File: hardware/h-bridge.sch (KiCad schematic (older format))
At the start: 78 parts, among them M1 MOUNTING_HOLE, M2 MOUNTING_HOLE, M3 MOUNTING_HOLE, M4 MOUNTING_HOLE, M5 MOUNTING_HOLE, M6 MOUNTING_HOLE, P10 CONN_01_BRK, P11 CONN_01_M+, P12 CONN_01_M-, P8 CONN_01_V+, P9 CONN_01_V-, Q10 PSMN021-100, Q3 IRFP4468, Q4 PSMN021-100, Q5 IRFP4468, Q6 IRFP4468, Q7 IRFP4468, Q8 IRFP4468, Q9 IRFP4468, U16 Si8045AA, U17 MIC4127, U18 MIC4127, U19 LM5102, U20 Si8045AA, U21 LM5102

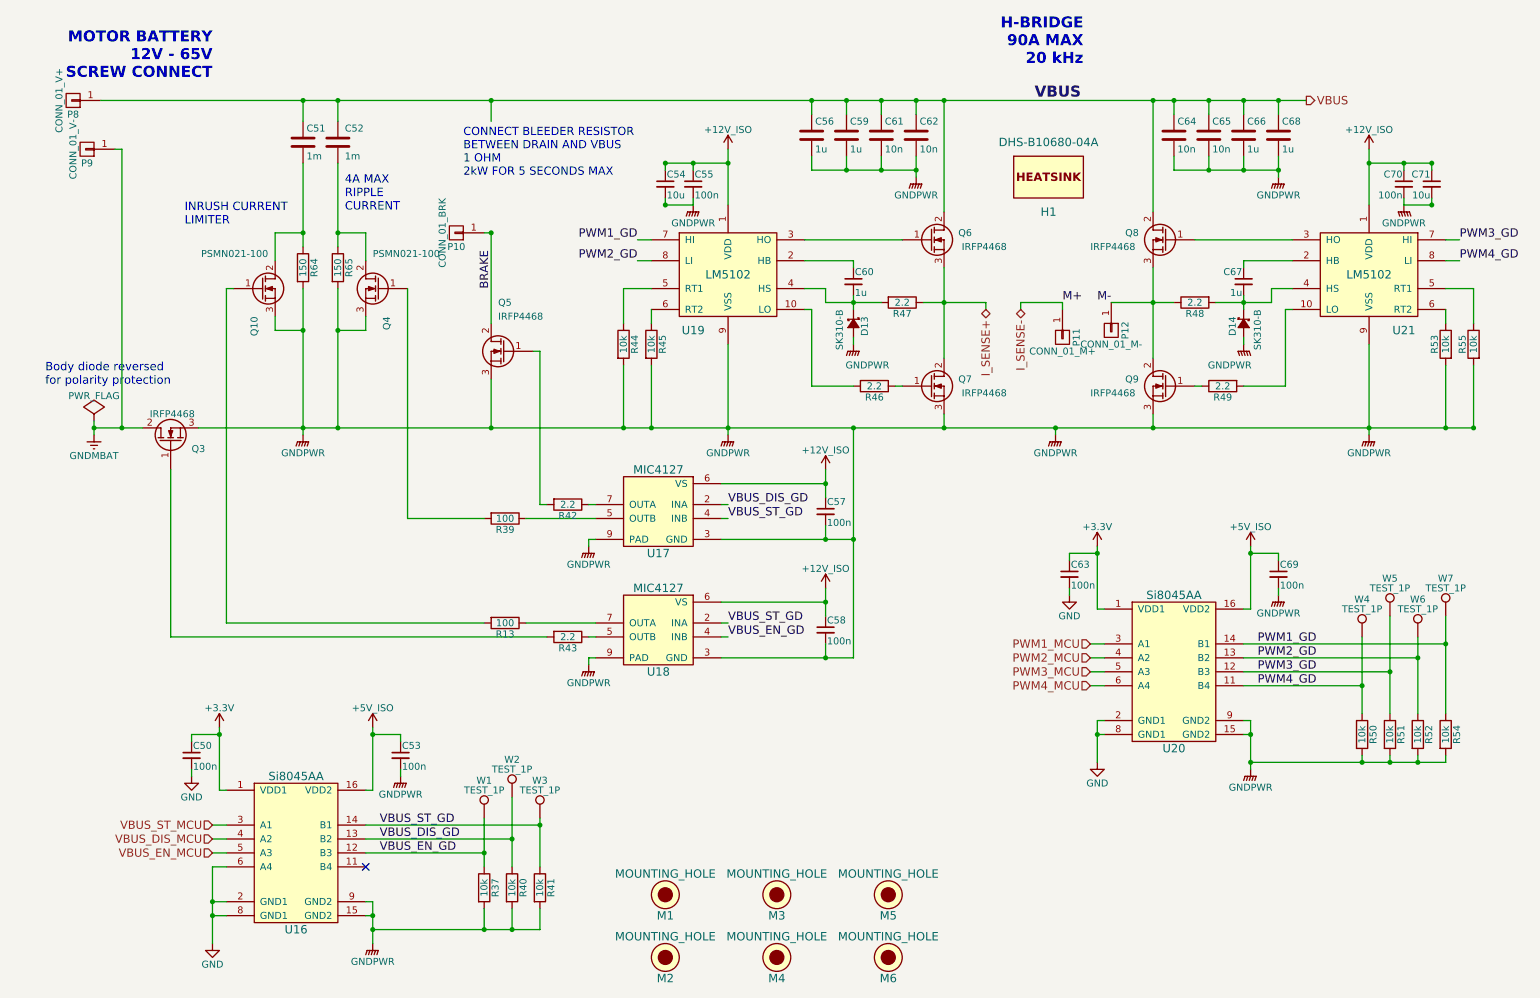
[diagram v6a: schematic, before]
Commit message: Gate driver layout mostly complete
- Gate driver layout
- Switch LM5102 for UCC27211 (higher current, more robust)
- Tweak gate drive circuit passives
- No soldermask on high-current traces
- Fix error in orientation of LAH-100P footprint
- Improved draft layout of control section
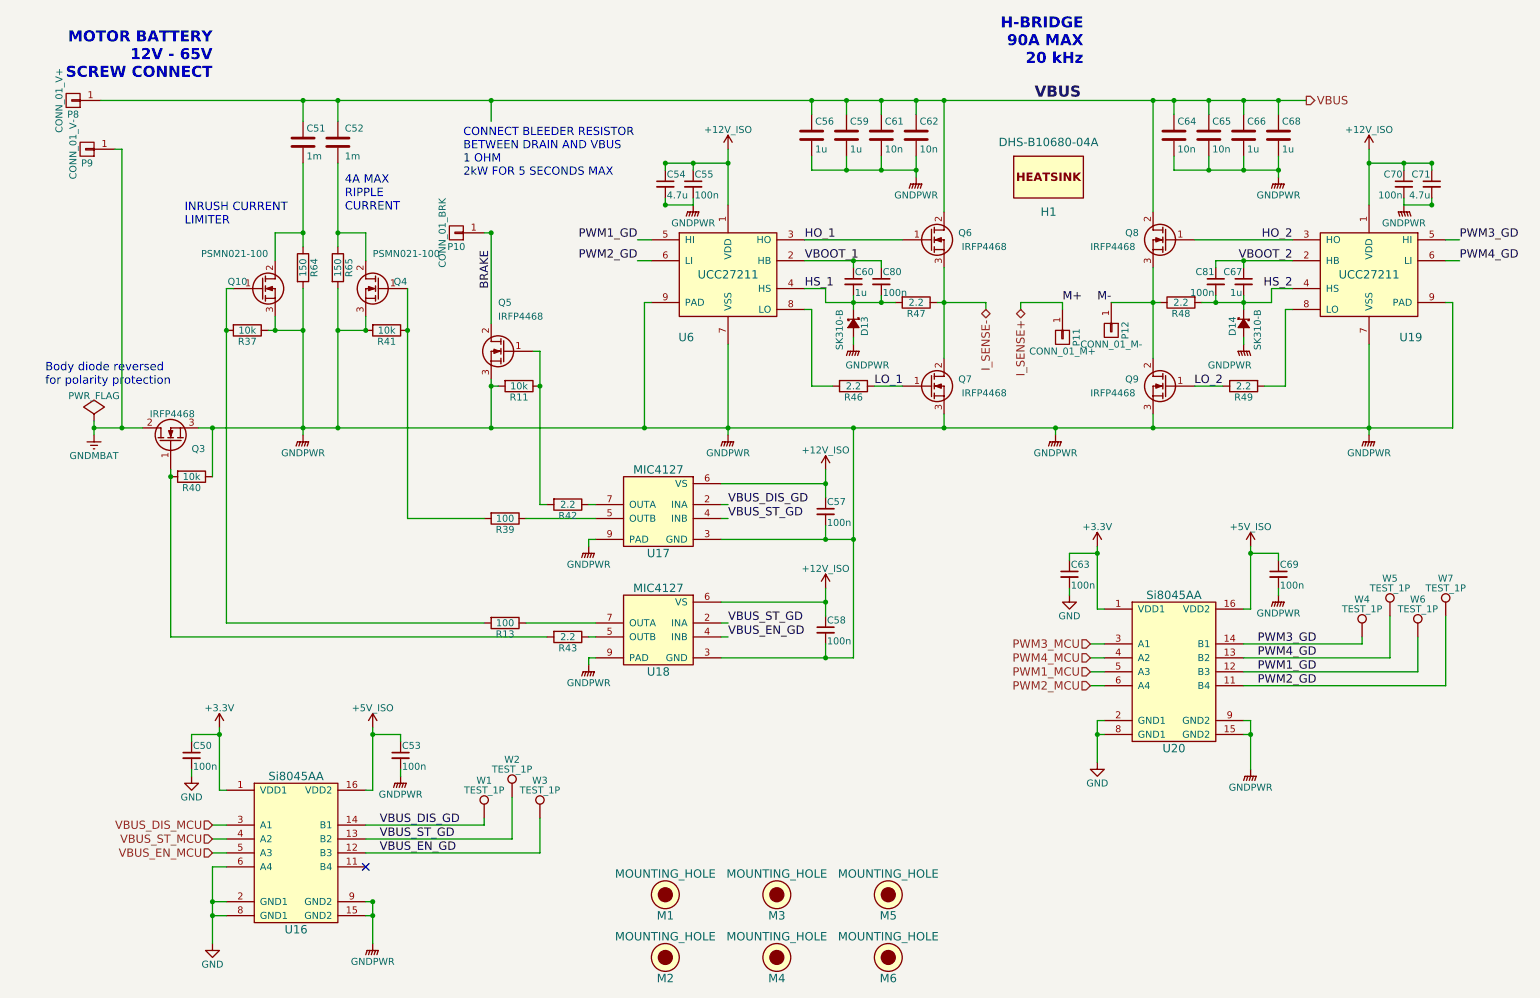
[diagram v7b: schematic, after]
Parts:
- removed R44, R45, R50, R51, R52, R53, R54, R55: 10k, Resistors_SMD:R_0603, symbol R
- removed U19, U21: LM5102, Housings_SSOP:MSOP-10_3x3mm_Pitch0.5mm, symbol LM5102
- added C80, C81: 100n, Capacitors_SMD:C_0603, symbol C_Small
- added R11: 10k, Resistors_SMD:R_0603, symbol R
- added U19, U6: UCC27211, Housings_SOIC:SOIC-8-1EP_3.9x4.9mm_Pitch1.27mm, symbol UCC27211
- C54, C71: value 10u -> 4.7u; footprint Capacitors_SMD:C_0603 -> Capacitors_SMD:C_0805
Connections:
- net +12V_ISO: now also U19.1 (VDD), U6.1 (VDD)
- net GNDPWR: now also R37.1, R40.1, R11.2, U19.7 (VSS), U19.9 (PAD), U6.7 (VSS), U6.9 (PAD); no longer R37.2, R40.2
- net I_SENSE+: now also P11.1 (P1); no longer Q6.3 (S), Q7.2 (D), R47.1
- net I_SENSE-: now also Q6.3 (S), Q7.2 (D), R47.1; no longer P11.1 (P1)
- net PWM1_GD: now also U20.12 (B3), W6.1, U6.5 (HI); no longer U20.14 (B1), W7.1
- net PWM1_MCU: now also U20.5 (A3); no longer U20.3 (A1)
- net PWM2_GD: now also U20.11 (B4), W7.1, U6.6 (LI); no longer U20.13 (B2), W6.1
- net PWM2_MCU: now also U20.6 (A4); no longer U20.4 (A2)
- net PWM3_GD: now also U20.14 (B1), W4.1, U19.5 (HI); no longer U20.12 (B3), W5.1
- net PWM3_MCU: now also U20.3 (A1); no longer U20.5 (A3)
- net PWM4_GD: now also U20.13 (B2), W5.1, U19.6 (LI); no longer U20.11 (B4), W4.1
- net PWM4_MCU: now also U20.4 (A2); no longer U20.6 (A4)
- net VBUS_DIS_GD: now also U16.14 (B1), W1.1; no longer R40.1, U16.13 (B2), W2.1
- net VBUS_DIS_MCU: now also U16.3 (A1); no longer U16.4 (A2)
- net VBUS_EN_GD: now also W3.1; no longer R37.1, W1.1
- net VBUS_ST_GD: now also U16.13 (B2), W2.1; no longer R41.1, U16.14 (B1), W3.1
- net VBUS_ST_MCU: now also U16.4 (A2); no longer U16.3 (A1)
- net HO_1: now reaches Q6.1 (G)
- net HO_1: now also U6.3 (HO)
- net LO_1: now reaches Q7.1 (G), R46.1
- net at R46.2: now also U6.8 (LO)
- net LO_2: now reaches Q9.1 (G), R49.1
- net HO_2: now reaches Q8.1 (G)
- net HO_2: now also U19.3 (HO)
- net at Q3.1 (G), R43.2: now also R40.2
- net at Q5.1 (G), R42.2: now also R11.1
- net VBOOT_1: now reaches C60.1
- net VBOOT_1: now also C80.1, U6.2 (HB)
- net HS_1: now reaches C60.2, D13.1 (K), R47.2
- net HS_1: now also C80.2, U6.4 (HS)
- net at R49.2: now also U19.8 (LO)
- net VBOOT_2: now reaches C67.1
- net VBOOT_2: now also C81.1, U19.2 (HB)
- net HS_2: now reaches C67.2, D14.1 (K), R48.2
- net HS_2: now also C81.2, U19.4 (HS)
- net at Q4.1 (G), R39.2: now also R41.1
- net at Q10.1 (G), R13.2: now also R37.2
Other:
- moved on the sheet: R37, R40, R41, R46, R47, R48, R49
